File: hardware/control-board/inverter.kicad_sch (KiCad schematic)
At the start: 26 parts, among them Q2 C3M0021120D, Q3 C3M0021120D, U3 UCC21550

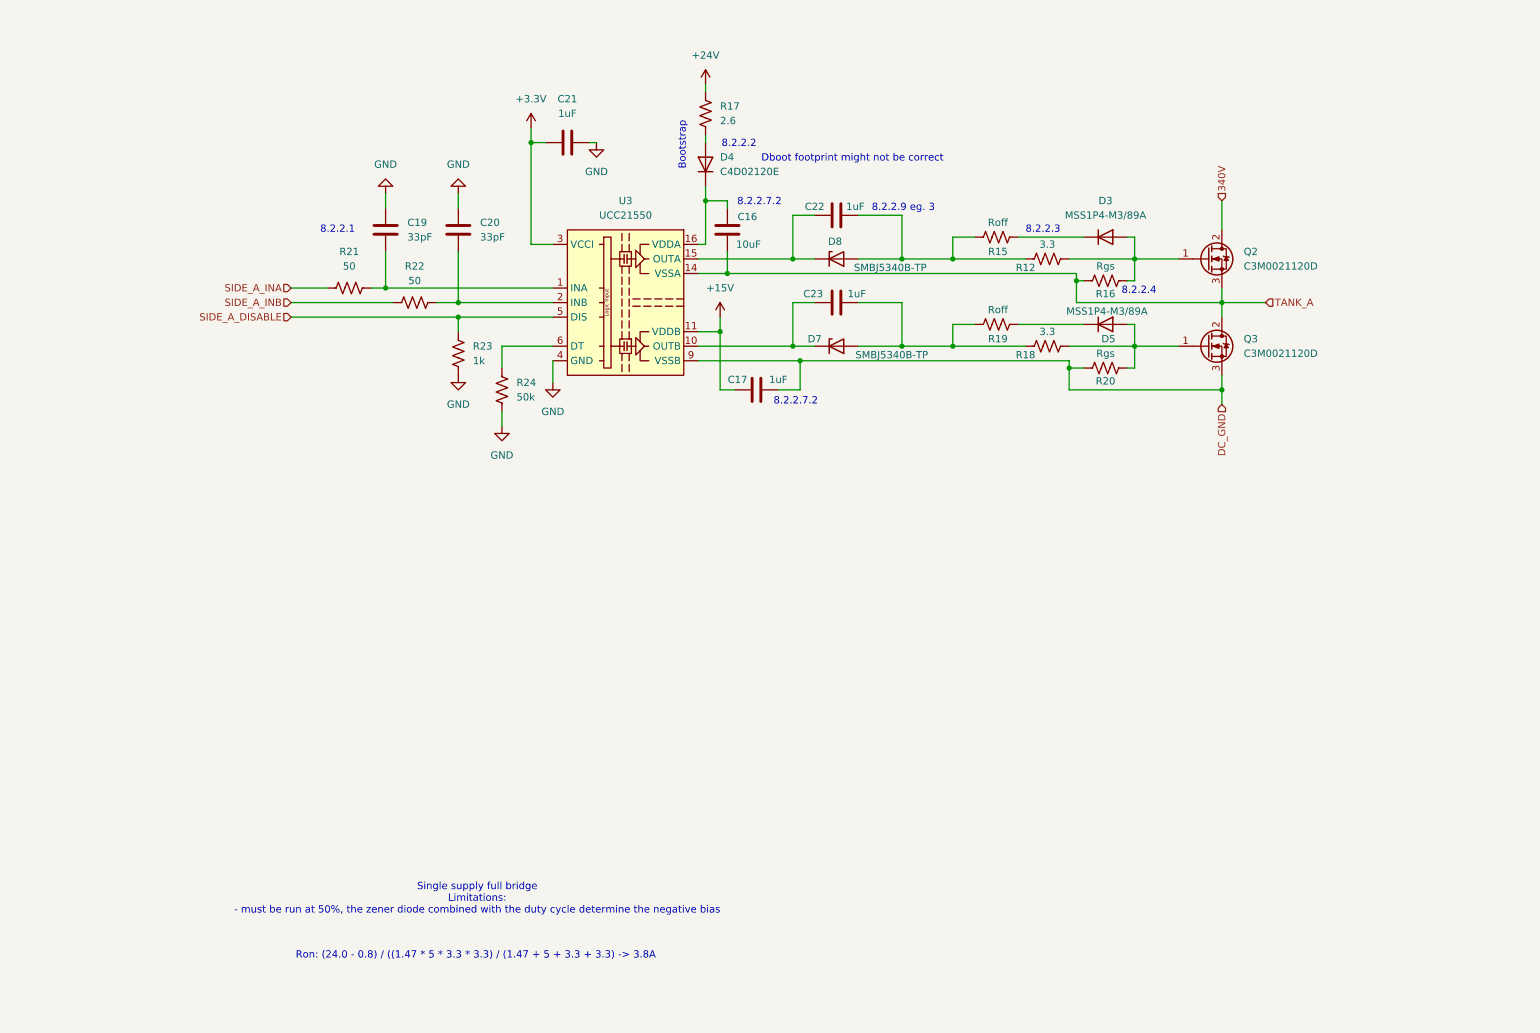
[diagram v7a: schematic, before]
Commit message: mirrored side a inverter to side b
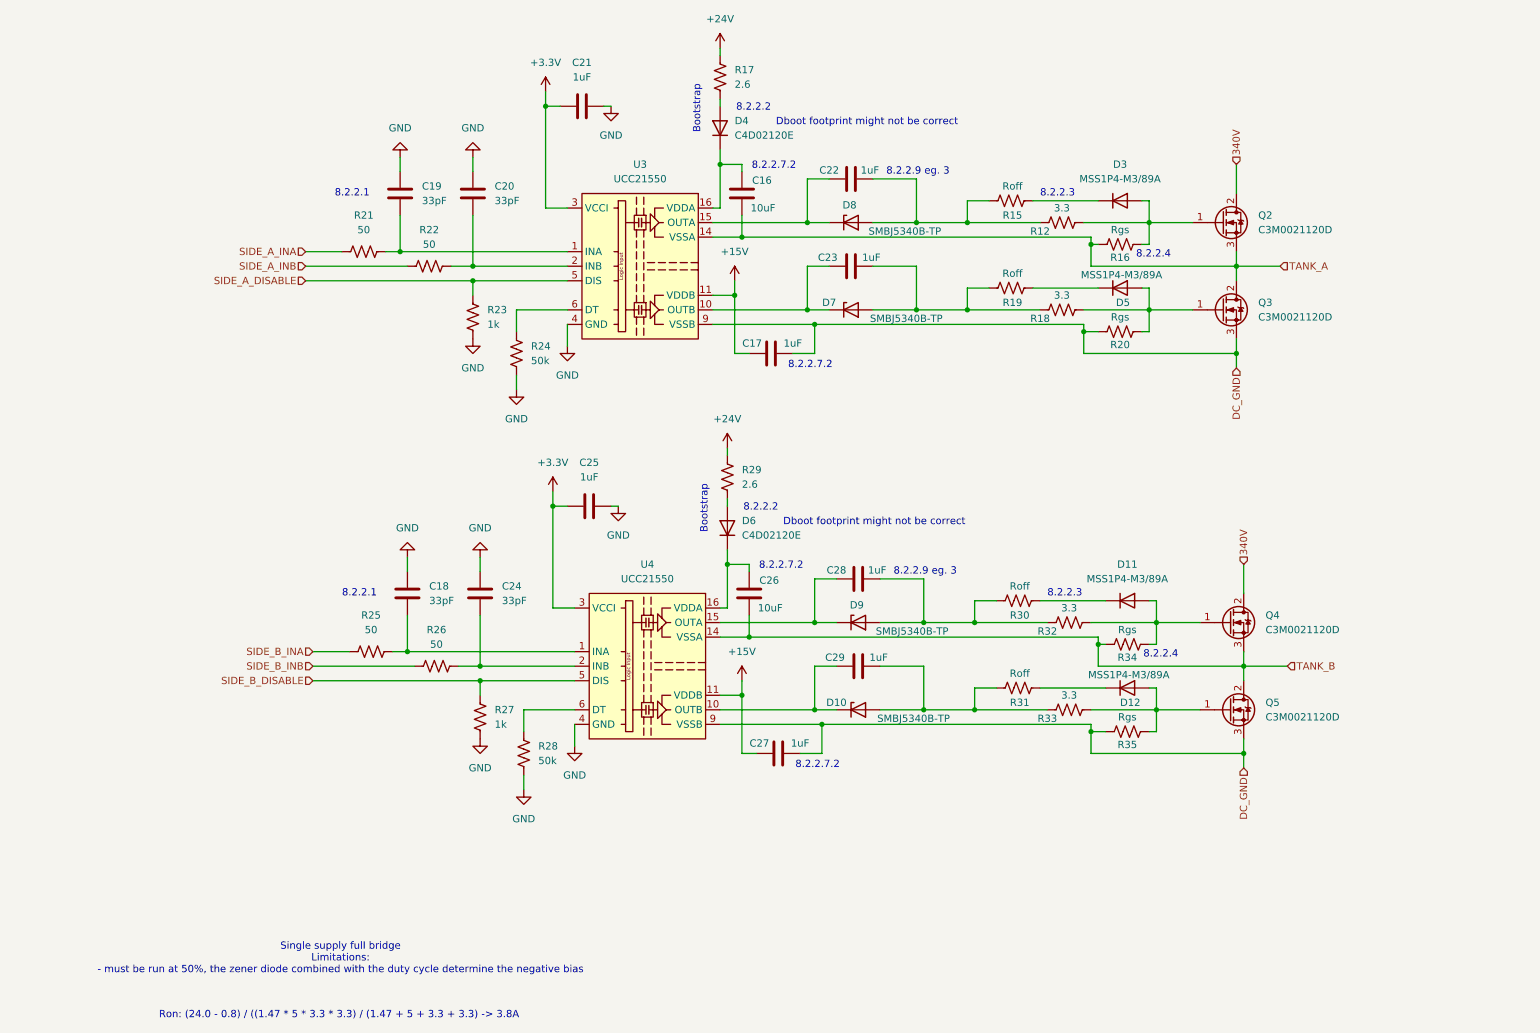
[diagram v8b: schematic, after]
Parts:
- added C18, C24: 33pF, Capacitor_SMD:C_0603_1608Metric, symbol Device:C
- added C25, C28, C29: 1uF, Capacitor_SMD:C_0603_1608Metric, symbol Device:C
- added C26: 10uF, Capacitor_SMD:C_0805_2012Metric, symbol Device:C
- added C27: 1uF, Capacitor_SMD:C_0805_2012Metric, symbol Device:C
- added D10, D9: SMBJ5340B-TP, Diode_SMD:D_SMB, symbol Device:D_Zener
- added D11, D12: MSS1P4-M3/89A, Diode_SMD:D_SMA, symbol Device:D
- added D6: C4D02120E, Package_TO_SOT_SMD:TO-252-2, symbol Device:D
- added Q4, Q5: C3M0021120D, Package_TO_SOT_THT:TO-247-3_Vertical, symbol sic_mosfet:C3M0021120D
- added R25, R26: 50, Resistor_SMD:R_0603_1608Metric, symbol Device:R_US
- added R27: 1k, Resistor_SMD:R_0603_1608Metric, symbol Device:R_US
- added R28: 50k, Resistor_SMD:R_0603_1608Metric, symbol Device:R_US
- added R29: 2.6, symbol Device:R_US
- added R30, R31: Roff, Resistor_SMD:R_2512_6332Metric, symbol Device:R_US
- added R32, R33: 3.3, Resistor_SMD:R_2512_6332Metric, symbol Device:R_US
- added R34, R35: Rgs, Resistor_SMD:R_0603_1608Metric, symbol Device:R_US
- added U4: UCC21550, Package_SO:SOIC-16W_7.5x10.3mm_P1.27mm, symbol gate_drivers:UCC21550
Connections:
- net +15V: now also C27.2, U4.11 (VDDB)
- net +24V: now also R29.1
- net +3.3V: now also C25.1, U4.3 (VCCI), U4.8 (VCCI)
- net 340V: now also Q4.2 (D)
- net DC_GND: now also C27.1, Q5.3 (S), R35.1, U4.9 (VSSB)
- net GND: now also C18.1, C24.1, C25.2, R27.1, R28.1, U4.4 (GND)
- new net: C28.1, D9.1 (K), U4.15 (OUTA)
- new net: C28.2, D9.2 (A), R30.1, R32.1
- new net: C26.1, D6.1 (K), U4.16 (VDDA)
- new net: D6.2 (A), R29.2
- new net: D11.2 (A), Q4.1 (G), R32.2, R34.2
- new net: C29.2, D10.2 (A), R31.1, R33.1
- new net: D12.1 (K), R31.2
- new net: C24.2, R26.2, U4.2 (INB)
- new net: D12.2 (A), Q5.1 (G), R33.2, R35.2
- new net: C29.1, D10.1 (K), U4.10 (OUTB)
- new net: R28.2, U4.6 (DT)
- new net: D11.1 (K), R30.2
- new net: C18.2, R25.2, U4.1 (INA)
- new net SIDE_B_DISABLE: R27.2, U4.5 (DIS)
- new net SIDE_B_INA: R25.1
- new net SIDE_B_INB: R26.1
- new net TANK_B: C26.2, Q4.3 (S), Q5.2 (D), R34.1, U4.14 (VSSA)
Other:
- moved on the sheet: C16, C17, C19, C20, C21, C22, C23, D3, D4, D5, D7, D8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
